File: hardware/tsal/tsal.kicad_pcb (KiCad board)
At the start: 2 copper layers, 81.9 x 74.9 mm, 66 parts, among them J1 Conn_01x02, J2 Conn_01x02, J3 Conn_01x02, J4 Conn_01x02, J5 Conn_01x03, J6 Conn_01x04, J7 Conn_01x02, Q1 BUK7M9R5-40H, Q2 BUK7M9R5-40H, U1 4081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

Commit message: Made some progress on the PCB
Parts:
- J1, J2, J3, J4, J7: footprint Connector_PinSocket_2.54mm:PinSocket_1x02_P2.54mm_Horizontal -> Connector_Molex:Molex_Micro-Fit_3.0_43650-0200_1x02_P3.00mm_Horizontal
- J5: footprint Connector_PinSocket_2.54mm:PinSocket_1x03_P2.54mm_Horizontal -> Connector_Molex:Molex_Micro-Fit_3.0_43650-0300_1x03_P3.00mm_Horizontal
- J6: footprint Connector_PinSocket_2.54mm:PinSocket_1x04_P2.54mm_Horizontal -> Connector_Molex:Molex_Micro-Fit_3.0_43650-0400_1x04_P3.00mm_Horizontal
- moved J6 15.4 mm to (69.2, 166.4), turned to 90 degrees
- moved J4 9.03 mm to (69.4, 148.8), turned to 90 degrees
- moved J3 8.57 mm to (69.4, 137.4), turned to 90 degrees
- moved J1 6.75 mm to (69.4, 121.5), turned to 90 degrees
- moved R14 0.90 mm to (123.8, 113.7), turned to 180 degrees
- moved J7 0.64 mm to (132.7, 158.1)
- moved Q1 0.64 mm to (102.9, 162.0)
- moved Q2 0.64 mm to (114.3, 162.0)
- moved D6 0.63 mm to (104.8, 156.9)
- moved D7 0.63 mm to (101.0, 156.9)
- moved D8 0.63 mm to (116.2, 156.9)
- moved D9 0.63 mm to (112.4, 156.9)
- moved R20 0.63 mm to (102.9, 146.7)
- moved R21 0.63 mm to (103.0, 151.2)
- moved R22 0.63 mm to (114.3, 146.7)
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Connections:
- U5 pad 12: /RED_LED_ON -> unconnected-(U5-Pad12)
- U5 pad 13: Net-(D5-Pad3) -> GND
- U7 pad 3: GND -> Net-(D5-Pad3)
- U7 pad 4: unconnected-(U7-Pad4) -> /RED_LED_ON
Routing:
- net /IMPLAUSIBLE: track 0.00 -> 46.6 mm, vias 0 -> 2
- net Net-(C5-Pad1): track 0.00 -> 46.5 mm
- net Net-(C2-Pad1): track 0.00 -> 46.1 mm, vias 0 -> 2
- net unconnected-(U5-Pad12): track 0.00 -> 40.4 mm, vias 0 -> 2
- net Net-(D5-Pad3): track 12.0 -> 51.6 mm, vias 0 -> 2
- net Net-(C3-Pad1): track 3.20 -> 34.3 mm, vias 0 -> 2
- net /~{PRCHG_MECH_ON}: track 0.00 -> 30.4 mm, vias 0 -> 4
- net Net-(U2-Pad3): track 0.00 -> 29.3 mm, vias 0 -> 2
- net GND: track 21.2 -> 47.7 mm, vias 1 -> 13
- net /HIGH_AIR_INTENDED_ON: track 0.00 -> 25.4 mm, vias 0 -> 2
- net Net-(C4-Pad1): track 0.00 -> 24.9 mm
- net Net-(U2-Pad4): track 0.00 -> 24.5 mm, vias 0 -> 2
- net Net-(R6-Pad1): track 0.00 -> 24.2 mm, vias 0 -> 2
- net Net-(R11-Pad1): track 0.00 -> 22.8 mm, vias 0 -> 2
- net Net-(D3-Pad1): track 0.00 -> 22.2 mm
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
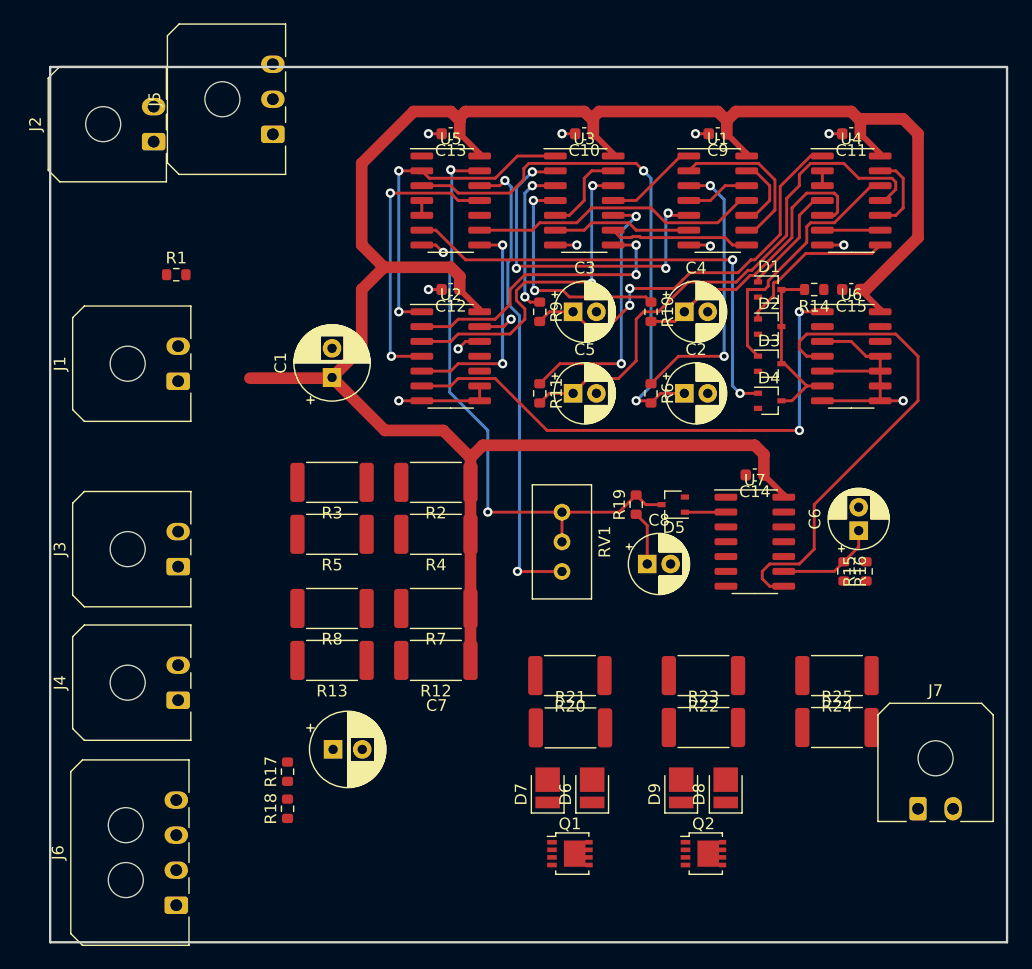
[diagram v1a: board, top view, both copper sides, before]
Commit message: Designed and finished layout of TSAL
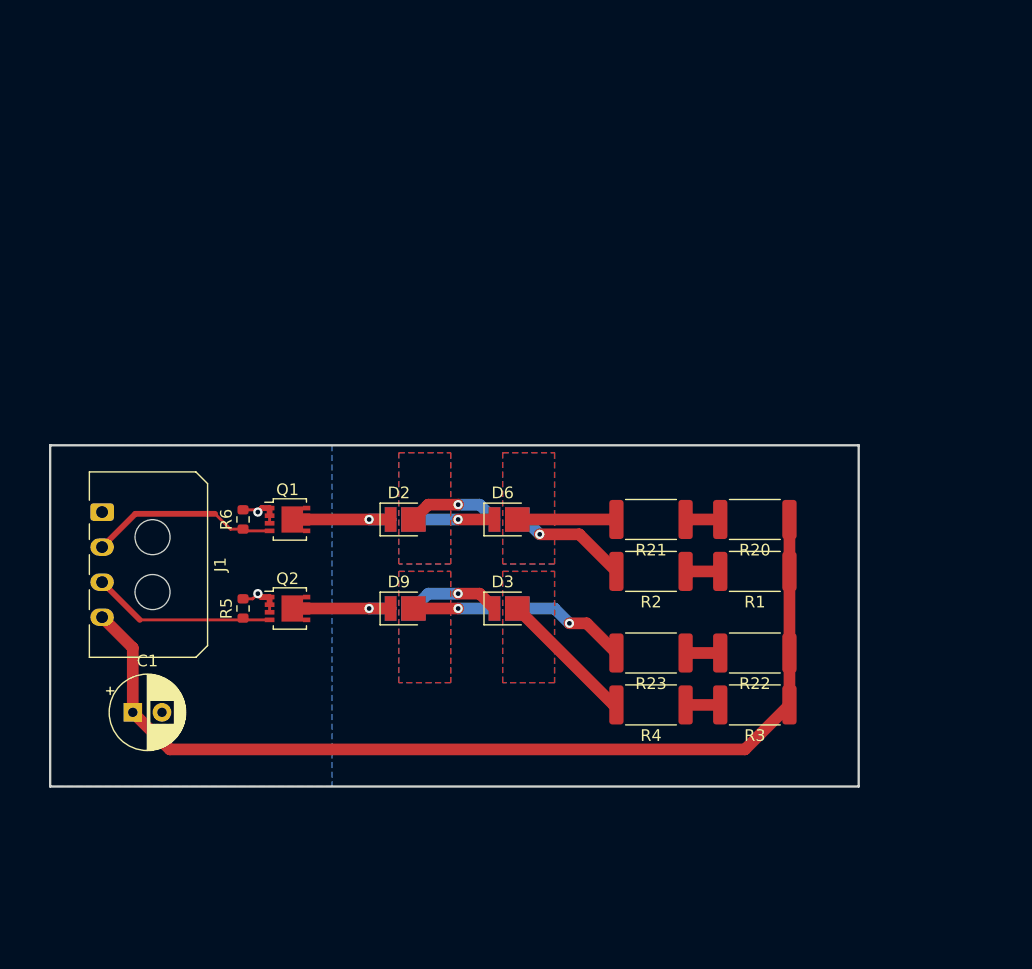
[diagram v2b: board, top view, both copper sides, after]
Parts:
- removed C10, C11, C12, C13, C14, C15, C9: 100n, Capacitor_SMD:C_0603_1608Metric
- removed C2, C3, C4, C5, C6, C8: 10u, Capacitor_THT:CP_Radial_D5.0mm_P2.00mm
- removed C7: 100u, Capacitor_THT:CP_Radial_D6.3mm_P2.50mm
- removed D5: BAT54W, Package_TO_SOT_SMD:SOT-323_SC-70
- removed J2, J3, J4, J7: Conn_01x02, Connector_Molex:Molex_Micro-Fit_3.0_43650-0200_1x02_P3.00mm_Horizontal
- removed J5: Conn_01x03, Connector_Molex:Molex_Micro-Fit_3.0_43650-0300_1x03_P3.00mm_Horizontal
- removed J6: Conn_01x04, Connector_Molex:Molex_Micro-Fit_3.0_43650-0400_1x04_P3.00mm_Horizontal
- removed R10, R11, R14, R15, R16, R17, R18, R19, R9: 10k, Resistor_SMD:R_0603_1608Metric
- removed R12, R13, R7, R8: 82, Resistor_SMD:R_2512_6332Metric
- removed R24, R25: 27, Resistor_SMD:R_2512_6332Metric
- removed RV1: 470k, Potentiometer_THT:Potentiometer_Bourns_3296W_Vertical
- removed U1, U3: 4081, Package_SO:SOIC-14_3.9x8.7mm_P1.27mm
- removed U2: 4071, Package_SO:SOIC-14_3.9x8.7mm_P1.27mm
- removed U4, U5, U7: 40106, Package_SO:SOIC-14_3.9x8.7mm_P1.27mm
- removed U6: 4013, Package_SO:SOIC-14_3.9x8.7mm_P1.27mm
- D1: value BAT54W -> 150283RS73103; footprint Package_TO_SOT_SMD:SOT-323_SC-70 -> footprints:Wurth_WL-SMTW; moved to B.Cu
- D2: value BAT54W -> 150283RS73103; footprint Package_TO_SOT_SMD:SOT-323_SC-70 -> footprints:Wurth_WL-SMTW
- D3: value BAT54W -> 150283GS73103; footprint Package_TO_SOT_SMD:SOT-323_SC-70 -> footprints:Wurth_WL-SMTW
- D4: value BAT54W -> 150283GS73103; footprint Package_TO_SOT_SMD:SOT-323_SC-70 -> footprints:Wurth_WL-SMTW; moved to B.Cu
- D7, D8: moved to B.Cu
- J1: value Conn_01x02 -> Conn_01x04; footprint Connector_Molex:Molex_Micro-Fit_3.0_43650-0200_1x02_P3.00mm_Horizontal -> Connector_Molex:Molex_Micro-Fit_3.0_43650-0400_1x04_P3.00mm_Horizontal
- R1: value 10k -> 27; footprint Resistor_SMD:R_0603_1608Metric -> Resistor_SMD:R_2512_6332Metric
- R2, R3, R4: value 82 -> 27
- R5: value 82 -> 10k; footprint Resistor_SMD:R_2512_6332Metric -> Resistor_SMD:R_0603_1608Metric
- R6: value 100k -> 10k
- moved R1 55.7 mm to (118.7, 137.8), turned to 180 degrees
- moved Q2 41.3 mm to (78.7, 141.0)
- moved R3 40.9 mm to (118.7, 149.2)
- moved Q1 37.5 mm to (78.7, 133.3)
- moved R6 36.6 mm to (74.9, 133.3), turned to 90 degrees
- moved D4 36.4 mm to (88.3, 141.0)
- moved D2 35.8 mm to (88.3, 133.3)
- moved C1 33.4 mm to (65.5, 149.9), turned to 0 degrees
- moved D3 31.0 mm to (97.2, 141.0)
- moved D1 30.2 mm to (97.2, 133.3)
- moved D9 28.9 mm to (88.3, 141.0), turned to 0 degrees
- moved D7 26.8 mm to (88.3, 133.3), turned to 0 degrees
- moved D8 24.9 mm to (97.2, 141.0), turned to 0 degrees
- moved D6 24.7 mm to (97.2, 133.3), turned to 0 degrees
- moved R4 23.5 mm to (109.9, 149.2)
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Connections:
- D1 pad 2: unconnected-(D1-Pad2) -> Net-(D1-Pad2)
- D2 pad 1: Net-(D2-Pad1) -> Net-(D7-Pad1)
- D2 pad 2: unconnected-(D2-Pad2) -> Net-(D1-Pad1)
- D3 pad 2: unconnected-(D3-Pad2) -> Net-(D3-Pad2)
- D4 pad 1: Net-(D4-Pad1) -> Net-(D9-Pad1)
- D4 pad 2: unconnected-(D4-Pad2) -> Net-(D3-Pad1)
- J1 pad 2: +12V -> /RED_LED_ON
- R1 pad 1: /~{PRCHG_MECH_ON} -> +12V
- R1 pad 2: +12V -> Net-(R1-Pad2)
- R2 pad 1: +12V -> Net-(R1-Pad2)
- R2 pad 2: Net-(R2-Pad2) -> Net-(D1-Pad2)
- R3 pad 1: Net-(R2-Pad2) -> +12V
- R3 pad 2: /~{LOW_AIR_MECH_ON} -> Net-(R3-Pad2)
- R4 pad 1: +12V -> Net-(R3-Pad2)
- R4 pad 2: Net-(R2-Pad2) -> Net-(D3-Pad2)
- R5 pad 1: Net-(R2-Pad2) -> /GREEN_LED_ON
- R5 pad 2: /~{LOW_AIR_MECH_ON} -> GND
- R6 pad 1: Net-(R6-Pad1) -> /RED_LED_ON
- R6 pad 2: Net-(C2-Pad1) -> GND
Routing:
- net +12V: track 186.7 -> 84.2 mm
- net Net-(D5-Pad3): track 51.6 -> 0.00 mm, vias 2 -> 0
- net /IMPLAUSIBLE: track 46.6 -> 0.00 mm, vias 2 -> 0
- net Net-(C5-Pad1): track 46.5 -> 0.00 mm
- net Net-(C2-Pad1): track 46.1 -> 0.00 mm, vias 2 -> 0
- net /POR: track 42.2 -> 0.00 mm
- net Net-(D4-Pad1): track 40.9 -> 0.00 mm, vias 2 -> 0
- net unconnected-(U5-Pad12): track 40.4 -> 0.00 mm, vias 2 -> 0
- net GND: track 47.7 -> 7.68 mm, vias 13 -> 2
- net Net-(C3-Pad1): track 34.3 -> 0.00 mm, vias 2 -> 0
- net /~{PRCHG_MECH_ON}: track 30.4 -> 0.00 mm, vias 4 -> 0
- net Net-(U2-Pad3): track 29.3 -> 0.00 mm, vias 2 -> 0
- net /PRCHG_INTENDED_ON: track 28.5 -> 0.00 mm, vias 2 -> 0
- net /HIGH_AIR_INTENDED_ON: track 25.4 -> 0.00 mm, vias 2 -> 0
- net Net-(U1-Pad11): track 25.0 -> 0.00 mm
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- added copper zone on F.Cu, net Net-(D1-Pad1)
- added copper zone on B.Cu, net Net-(D1-Pad2)
- added copper zone on B.Cu, net Net-(D3-Pad1)
- added copper zone on F.Cu, net Net-(D3-Pad2)
- added copper zone on B.Cu, net Net-(D6-Pad1)
- added copper zone on F.Cu, net Net-(D6-Pad2)
- added copper zone on F.Cu, net Net-(D8-Pad1)
- added copper zone on B.Cu, net Net-(D8-Pad2)
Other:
- board size 81.9 x 74.9 mm -> 69.2 x 29.2 mm

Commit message: Fixed references
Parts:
- moved J1 10.4 mm to (68.1, 141.7), turned to 90 degrees
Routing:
- net +12V: track 84.2 -> 101.3 mm
- net /RED_LED_ON: track 16.1 -> 11.0 mm
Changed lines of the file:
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@@
     (property "Sheetname" "")
     (attr smd)
-    (fp_text reference "R20" (at 0 -2.62) (layer "F.SilkS")
+    (fp_text reference "R20" (at 0 2.54) (layer "F.SilkS")
       (effects (font (size 1 1) (thickness 0.15)))
     )
@@
     (solder_mask_margin 0.05)
     (attr smd)
-    (fp_text reference "Q1" (at 0 -2.55) (layer "F.SilkS")
+    (fp_text reference "Q1" (at 0.254 2.54) (layer "F.SilkS")
       (effects (font (size 1 1) (thickness 0.15)))
     )
@@
   )
   (footprint "Connector_Molex:Molex_Micro-Fit_3.0_43650-0400_1x04_P3.00mm_Horizontal" (layer "F.Cu")
-    (at 62.865 132.715 -90)
+    (at 68.105 141.715 90)
     (descr "Molex Micro-Fit 3.0 Connector System, 43650-0400 (compatible alternatives: 43650-0401, 43650-0402), 4 Pins per row (https://www.molex.com/pdm_docs/sd/436500300_sd.pdf), generated with kicad-footprint-generator")
     (tags "connector Molex Micro-Fit_3.0 top entry")
@@
     (property "Sheetname" "")
     (attr through_hole)
-    (fp_text reference "J1" (at 4.5 -10.12 90) (layer "F.SilkS")
+    (fp_text reference "J1" (at -5.097 -8.03 180) (layer "F.SilkS")
       (effects (font (size 1 1) (thickness 0.15)))
     )
@@
     (fp_line (start 11.325 -8.92) (end 12.325 -7.92) (layer "F.Fab") (width 0.1))
     (fp_line (start -2.325 -8.92) (end 11.325 -8.92) (layer "F.Fab") (width 0.1))
-    (pad "" np_thru_hole circle (at 6.85 -4.32 270) (size 3 3) (drill 3) (layers *.Cu *.Mask))
-    (pad "" np_thru_hole circle (at 2.15 -4.32 270) (size 3 3) (drill 3) (layers *.Cu *.Mask))
-    (pad "1" thru_hole roundrect (at 0 0 270) (size 1.5 2.02) (drill 1.02) (layers *.Cu *.Mask) (roundrect_rratio 0.166667)
+    (pad "" np_thru_hole circle (at 6.85 -4.32 90) (size 3 3) (drill 3) (layers *.Cu *.Mask))
+    (pad "" np_thru_hole circle (at 2.15 -4.32 90) (size 3 3) (drill 3) (layers *.Cu *.Mask))
+    (pad "1" thru_hole roundrect (at 0 0 90) (size 1.5 2.02) (drill 1.02) (layers *.Cu *.Mask) (roundrect_rratio 0.166667)
       (net 2 "GND") (pinfunction "Pin_1") (pintype "passive"))
-    (pad "2" thru_hole oval (at 3 0 270) (size 1.5 2.02) (drill 1.02) (layers *.Cu *.Mask)
+    (pad "2" thru_hole oval (at 3 0 90) (size 1.5 2.02) (drill 1.02) (layers *.Cu *.Mask)
       (net 15 "/RED_LED_ON") (pinfunction "Pin_2") (pintype "passive"))
-    (pad "3" thru_hole oval (at 6 0 270) (size 1.5 2.02) (drill 1.02) (layers *.Cu *.Mask)
+    (pad "3" thru_hole oval (at 6 0 90) (size 1.5 2.02) (drill 1.02) (layers *.Cu *.Mask)
       (net 16 "/GREEN_LED_ON") (pinfunction "Pin_3") (pintype "passive"))
-    (pad "4" thru_hole oval (at 9 0 270) (size 1.5 2.02) (drill 1.02) (layers *.Cu *.Mask)
+    (pad "4" thru_hole oval (at 9 0 90) (size 1.5 2.02) (drill 1.02) (layers *.Cu *.Mask)
       (net 1 "+12V") (pinfunction "Pin_4") (pintype "passive"))
     (model "${KICAD6_3DMODEL_DIR}/Connector_Molex.3dshapes/Molex_Micro-Fit_3.0_43650-0400_1x04_P3.00mm_Horizontal.wrl"
@@
     (property "Sheetname" "")
     (attr smd)
-    (fp_text reference "R5" (at 0 -1.43 90) (layer "F.SilkS")
+    (fp_text reference "R5" (at -2.286 0 180) (layer "F.SilkS")
       (effects (font (size 1 1) (thickness 0.15)))
     )
@@
     (property "Sheetname" "")
     (attr smd)
-    (fp_text reference "R22" (at 0 -2.62) (layer "F.SilkS")
+    (fp_text reference "R22" (at 0 2.54) (layer "F.SilkS")
       (effects (font (size 1 1) (thickness 0.15)))
     )
@@
     (property "Sheetname" "")
     (attr smd)
-    (fp_text reference "R23" (at 0 -2.62) (layer "F.SilkS")
+    (fp_text reference "R23" (at 0 2.54) (layer "F.SilkS")
       (effects (font (size 1 1) (thickness 0.15)))
     )
@@
     (property "Sheetname" "")
     (attr smd)
-    (fp_text reference "R21" (at 0 -2.62) (layer "F.SilkS")
+    (fp_text reference "R21" (at 0 2.54) (layer "F.SilkS")
       (effects (font (size 1 1) (thickness 0.15)))
     )
@@
     (property "Sheetname" "")
     (attr smd)
-    (fp_text reference "R6" (at 0 -1.43 90) (layer "F.SilkS")
+    (fp_text reference "R6" (at -2.286 0.254 180) (layer "F.SilkS")
       (effects (font (size 1 1) (thickness 0.15)))
     )
@@
     (solder_mask_margin 0.05)
     (attr smd)
-    (fp_text reference "Q2" (at 0 -2.55) (layer "F.SilkS")
+    (fp_text reference "Q2" (at 0 2.667) (layer "F.SilkS")
       (effects (font (size 1 1) (thickness 0.15)))
     )
@@
     (property "Sheetname" "")
     (attr through_hole)
-    (fp_text reference "C1" (at 1.25 -4.4) (layer "F.SilkS")
+    (fp_text reference "C1" (at 4.992379 -2.54) (layer "F.SilkS")
       (effects (font (size 1 1) (thickness 0.15)))
     )
@@
   )
   (gr_rect (start 58.42 127) (end 127.635 156.21) (layer "Edge.Cuts") (width 0.2) (fill none))
-  (segment (start 65.492621 144.342621) (end 62.865 141.715) (width 1) (layer "F.Cu") (net 1))
   (segment (start 121.7075 149.225) (end 117.8975 153.035) (width 1) (layer "F.Cu") (net 1))
   (segment (start 121.7075 137.795) (end 121.7075 144.78) (width 1) (layer "F.Cu") (net 1))
@@
   (segment (start 68.667621 153.035) (end 65.492621 149.86) (width 1) (layer "F.Cu") (net 1))
   (segment (start 117.8975 153.035) (end 68.667621 153.035) (width 1) (layer "F.Cu") (net 1))
+  (segment (start 67.47 132.08) (end 62.23 132.08) (width 1) (layer "F.Cu") (net 1))
+  (segment (start 62.23 132.08) (end 60.96 133.35) (width 1) (layer "F.Cu") (net 1))
+  (segment (start 60.96 145.327379) (end 65.492621 149.86) (width 1) (layer "F.Cu") (net 1))
   (segment (start 121.7075 133.35) (end 121.7075 137.795) (width 1) (layer "F.Cu") (net 1))
-  (segment (start 65.492621 149.86) (end 65.492621 144.342621) (width 1) (layer "F.Cu") (net 1))
+  (segment (start 68.105 132.715) (end 67.47 132.08) (width 1) (layer "F.Cu") (net 1))
+  (segment (start 60.96 133.35) (end 60.96 145.327379) (width 1) (layer "F.Cu") (net 1))
   (segment (start 77.205 139.995) (end 76.495 139.995) (width 0.5) (layer "F.Cu") (net 2))
   (segment (start 77.205 132.375) (end 76.54 132.375) (width 0.5) (layer "F.Cu") (net 2))
@@
   (via (at 85.725 140.97) (size 0.8) (drill 0.4) (layers "F.Cu" "B.Cu") (net 14))
   (segment (start 87.565 140.97) (end 85.725 140.97) (width 1) (layer "B.Cu") (net 14))
-  (segment (start 72.540479 132.865479) (end 73.85 134.175) (width 0.25) (layer "F.Cu") (net 15))
+  (segment (start 70.39 138.715) (end 68.105 138.715) (width 0.25) (layer "F.Cu") (net 15))
   (segment (start 75.08 134.325) (end 77.205 134.325) (width 0.25) (layer "F.Cu") (net 15))
   (segment (start 74.93 134.175) (end 75.08 134.325) (width 0.25) (layer "F.Cu") (net 15))
-  (segment (start 65.714521 132.865479) (end 72.540479 132.865479) (width 0.5) (layer "F.Cu") (net 15))
-  (segment (start 73.85 134.175) (end 74.93 134.175) (width 0.25) (layer "F.Cu") (net 15))
-  (segment (start 62.865 135.715) (end 65.714521 132.865479) (width 0.5) (layer "F.Cu") (net 15))
+  (segment (start 74.93 134.175) (end 70.39 138.715) (width 0.25) (layer "F.Cu") (net 15))
   (segment (start 74.93 141.795) (end 75.08 141.945) (width 0.25) (layer "F.Cu") (net 16))
+  (segment (start 66.675 139.7) (end 67.31 140.335) (width 0.25) (layer "F.Cu") (net 16))
+  (segment (start 68.105 135.715) (end 66.675 137.145) (width 0.25) (layer "F.Cu") (net 16))
   (segment (start 74.78 141.945) (end 74.93 141.795) (width 0.25) (layer "F.Cu") (net 16))
   (segment (start 75.08 141.945) (end 77.205 141.945) (width 0.25) (layer "F.Cu") (net 16))
-  (segment (start 62.865 138.715) (end 66.095 141.945) (width 0.5) (layer "F.Cu") (net 16))
-  (segment (start 66.095 141.945) (end 74.78 141.945) (width 0.25) (layer "F.Cu") (net 16))
+  (segment (start 73.47 140.335) (end 74.93 141.795) (width 0.25) (layer "F.Cu") (net 16))
+  (segment (start 66.675 137.145) (end 66.675 139.7) (width 0.25) (layer "F.Cu") (net 16))
+  (segment (start 67.31 140.335) (end 73.47 140.335) (width 0.25) (layer "F.Cu") (net 16))
   (segment (start 112.8175 133.35) (end 115.7825 133.35) (width 1) (layer "F.Cu") (net 17))
   (segment (start 112.8175 144.78) (end 115.7825 144.78) (width 1) (layer "F.Cu") (net 18))
